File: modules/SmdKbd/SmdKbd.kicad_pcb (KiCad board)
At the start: 2 copper layers, 40.6 x 40.6 mm, 28 parts, among them J1 Conn_01x10_Male, J2 Conn_01x10_Male, SW1 SW_Push, SW10 SW_Push, SW11 SW_Push, SW12 SW_Push, SW13 SW_Push, SW14 SW_Push, SW15 SW_Push, SW16 SW_Push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

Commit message: SmdKbd in work
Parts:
- moved SW15 0.71 mm to (114.0, 85.7)
- moved SW13 0.64 mm to (94.6, 85.7)
- turned SW11 to 270 degrees
- turned SW3 to 270 degrees
- turned SW6 to 90 degrees
- turned SW8 to 90 degrees
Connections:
- SW1 pad 2: Net-(SW1-Pad2) -> /A3
- SW13 pad 2: Net-(SW13-Pad2) -> /A3
- SW14 pad 2: Net-(SW14-Pad2) -> Net-(SW10-Pad2)
- SW15 pad 2: Net-(SW15-Pad2) -> Net-(SW11-Pad2)
- SW16 pad 2: Net-(SW16-Pad2) -> Net-(SW12-Pad2)
- SW2 pad 2: Net-(SW2-Pad2) -> Net-(SW10-Pad2)
- SW3 pad 2: Net-(SW3-Pad2) -> Net-(SW11-Pad2)
- SW4 pad 2: Net-(SW4-Pad2) -> Net-(SW12-Pad2)
- SW5 pad 2: Net-(SW5-Pad2) -> /A3
- SW6 pad 2: Net-(SW6-Pad2) -> Net-(SW10-Pad2)
- SW7 pad 2: Net-(SW7-Pad2) -> Net-(SW11-Pad2)
- SW8 pad 2: Net-(SW8-Pad2) -> Net-(SW12-Pad2)
- SW9 pad 2: Net-(SW9-Pad2) -> /A3
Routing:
- net GND: track 0.00 -> 83.4 mm
- net /5: track 0.00 -> 53.2 mm
- net /A3: track 0.00 -> 24.4 mm, vias 0 -> 1
- net Net-(SW12-Pad2): track 0.00 -> 22.8 mm
- net Net-(SW10-Pad2): track 0.00 -> 22.7 mm
- net Net-(D3-Pad2): track 0.00 -> 19.7 mm, vias 0 -> 1
- net Net-(SW11-Pad2): track 0.00 -> 18.0 mm
- net Net-(D5-Pad2): track 0.00 -> 13.0 mm, vias 0 -> 1
- net Net-(D8-Pad2): track 0.00 -> 9.32 mm, vias 0 -> 1
- net Net-(D6-Pad2): track 0.00 -> 8.97 mm, vias 0 -> 1
- net Net-(D7-Pad2): track 0.00 -> 7.61 mm, vias 0 -> 1
- net Net-(D2-Pad2): track 0.00 -> 7.31 mm, vias 0 -> 1

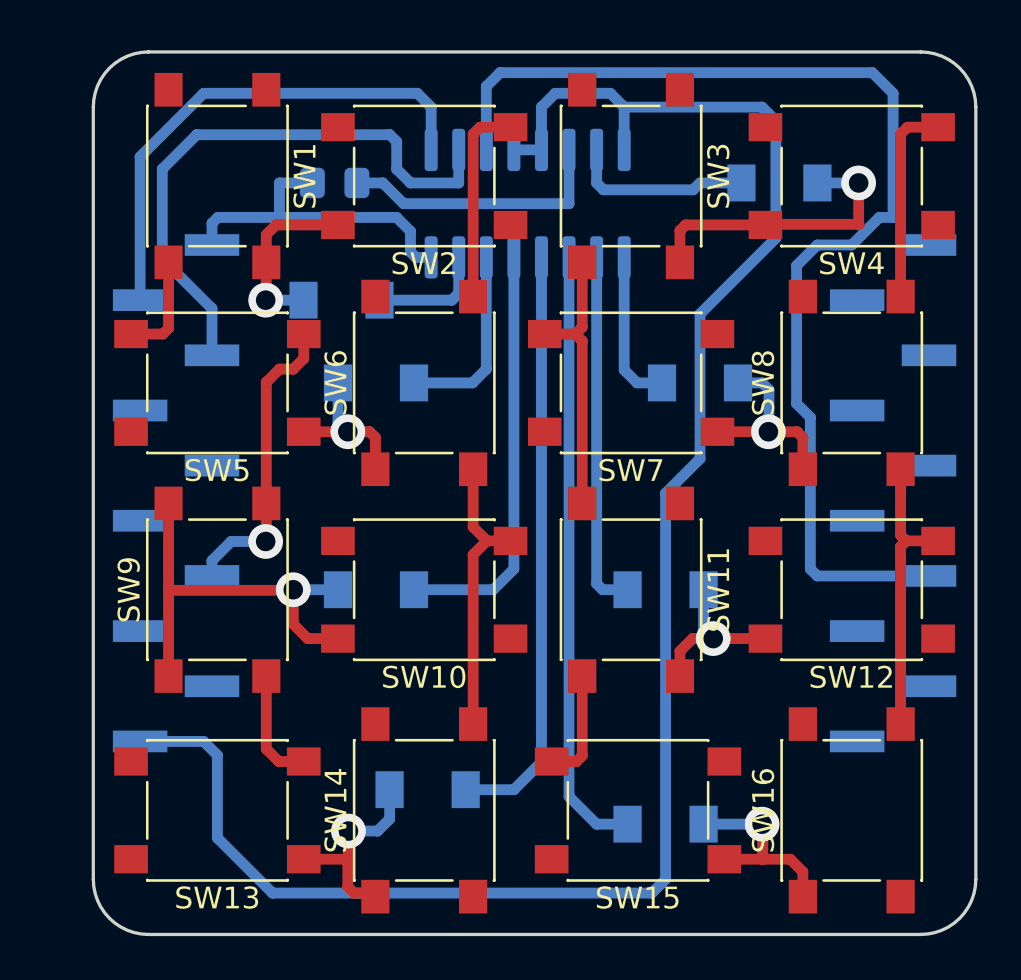
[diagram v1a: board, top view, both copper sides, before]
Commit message: All 1x shields was rotated clockwise
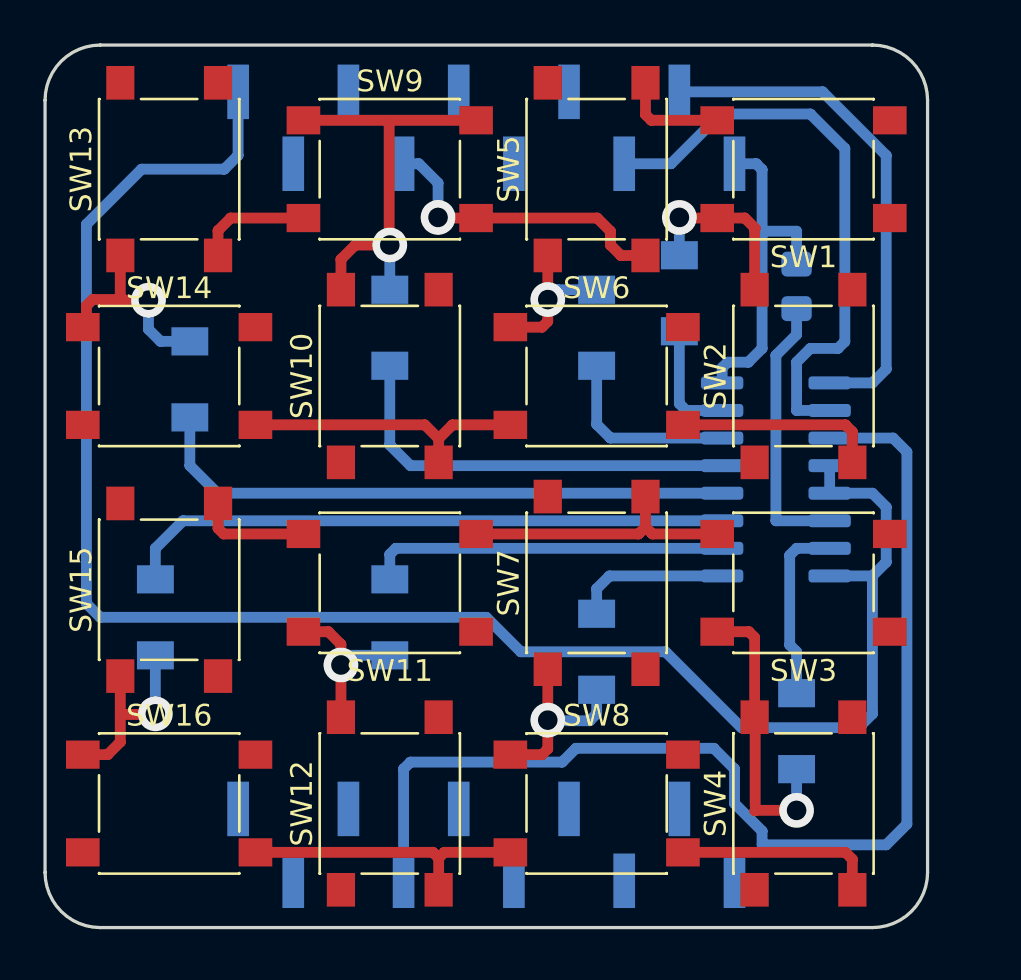
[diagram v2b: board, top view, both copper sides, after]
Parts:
- moved SW16 31.4 mm to (92.4, 85.4), turned to 0 degrees
- moved SW13 29.6 mm to (92.4, 56.2), turned to 90 degrees
- moved SW4 29.0 mm to (121.6, 85.4), turned to 90 degrees
- moved SW1 27.0 mm to (121.6, 56.2), turned to 180 degrees
- moved D8 25.4 mm to (91.8, 76.8), turned to 270 degrees
- moved D5 25.3 mm to (121.3, 82.1), turned to 270 degrees
- moved J1 24.8 mm to (107.0, 87.3), turned to 270 degrees
- moved SW15 23.9 mm to (92.4, 75.6), turned to 90 degrees
- moved SW12 23.4 mm to (102.6, 85.4), turned to 90 degrees
- moved SW14 23.2 mm to (92.4, 65.7), turned to 0 degrees
- moved SW8 22.7 mm to (112.1, 85.4), turned to 0 degrees
- moved J2 22.1 mm to (107.0, 54.3), turned to 270 degrees
- moved D4 21.8 mm to (93.3, 65.9), turned to 90 degrees
- moved R1 21.8 mm to (121.3, 61.6), turned to 90 degrees
- moved SW9 20.9 mm to (102.6, 56.2), turned to 0 degrees
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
